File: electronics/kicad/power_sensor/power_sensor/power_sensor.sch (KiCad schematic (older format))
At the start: 6 parts, among them P4 a

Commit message: Spectrum analyzer progress
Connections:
- net at C?.1, R?.2: no longer D?.3
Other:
- moved on the sheet: C?, D?, P4, R?
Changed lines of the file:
@@
 L power:GND #PWR?
 U 1 1 5F014890
-P 5450 2300
-F 0 "#PWR?" H 5450 2300 30  0001 C CNN
-F 1 "GND" H 5450 2230 30  0001 C CNN
-F 2 "" H 5450 2300 50  0001 C CNN
-F 3 "" H 5450 2300 50  0001 C CNN
-	1    5450 2300
+P 5300 1750
+F 0 "#PWR?" H 5300 1750 30  0001 C CNN
+F 1 "GND" H 5300 1680 30  0001 C CNN
+F 2 "" H 5300 1750 50  0001 C CNN
+F 3 "" H 5300 1750 50  0001 C CNN
+	1    5300 1750
 	0    1    1    0
 $EndComp
@@
 L SparkFun-Capacitors:6PF-0402-50V-0.5% C?
 U 1 1 5F01536C
-P 6250 2500
-F 0 "C?" H 6358 2592 45  0000 L CNN
-F 1 "1 nF" H 6358 2508 45  0000 L CNN
-F 2 "0402" H 6250 2750 20  0001 C CNN
-F 3 "" H 6250 2500 50  0001 C CNN
-F 4 "" H 6358 2466 60  0000 L CNN "Field4"
-	1    6250 2500
+P 6100 1950
+F 0 "C?" H 6208 2042 45  0000 L CNN
+F 1 "1 nF" H 6208 1958 45  0000 L CNN
+F 2 "0402" H 6100 2200 20  0001 C CNN
+F 3 "" H 6100 1950 50  0001 C CNN
+F 4 "" H 6208 1916 60  0000 L CNN "Field4"
+	1    6100 1950
 	1    0    0    -1
 $EndComp
@@
 L power:GND #PWR?
 U 1 1 5F016B90
-P 6250 2600
-F 0 "#PWR?" H 6250 2600 30  0001 C CNN
-F 1 "GND" H 6250 2530 30  0001 C CNN
-F 2 "" H 6250 2600 50  0001 C CNN
-F 3 "" H 6250 2600 50  0001 C CNN
-	1    6250 2600
+P 6100 2050
+F 0 "#PWR?" H 6100 2050 30  0001 C CNN
+F 1 "GND" H 6100 1980 30  0001 C CNN
+F 2 "" H 6100 2050 50  0001 C CNN
+F 3 "" H 6100 2050 50  0001 C CNN
+	1    6100 2050
 	1    0    0    -1
 $EndComp
@@
 L conn:CONN_1 P4
 U 1 1 5EBA8EF1
-P 5750 2950
-F 0 "P4" H 5683 2853 40  0000 C CNN
-F 1 "a" H 5700 2990 30  0001 C CNN
-F 2 "TestPoint:TestPoint_Pad_1.5x1.5mm" H 5750 2950 50  0001 C CNN
-F 3 "" H 5750 2950 50  0001 C CNN
-	1    5750 2950
+P 5600 2950
+F 0 "P4" H 5533 2853 40  0000 C CNN
+F 1 "a" H 5550 2990 30  0001 C CNN
+F 2 "TestPoint:TestPoint_Pad_1.5x1.5mm" H 5600 2950 50  0001 C CNN
+F 3 "" H 5600 2950 50  0001 C CNN
+	1    5600 2950
 	0    1    1    0
 $EndComp
 Wire Wire Line
-	6250 2300 6050 2300
-Connection ~ 6250 2300
+	6100 1750 5900 1750
+Connection ~ 6100 1750
 $Comp
 L SparkFun-Resistors:RESISTOR0402 R?
 U 1 1 5F0217ED
-P 6700 2500
-F 0 "R?" V 6605 2568 45  0000 L CNN
-F 1 "10k" V 6689 2568 45  0000 L CNN
-F 2 "0402" H 6700 2650 20  0001 C CNN
-F 3 "" H 6700 2500 60  0001 C CNN
-F 4 " " V 6784 2568 60  0000 L CNN "Field4"
-	1    6700 2500
+P 6550 1950
+F 0 "R?" V 6455 2018 45  0000 L CNN
+F 1 "10k" V 6539 2018 45  0000 L CNN
+F 2 "0402" H 6550 2100 20  0001 C CNN
+F 3 "" H 6550 1950 60  0001 C CNN
+F 4 " " V 6634 2018 60  0000 L CNN "Field4"
+	1    6550 1950
 	0    1    1    0
 $EndComp
@@
 L power:GND #PWR?
 U 1 1 5F021FD0
-P 6700 2700
-F 0 "#PWR?" H 6700 2700 30  0001 C CNN
-F 1 "GND" H 6700 2630 30  0001 C CNN
-F 2 "" H 6700 2700 50  0001 C CNN
-F 3 "" H 6700 2700 50  0001 C CNN
-	1    6700 2700
+P 6550 2150
+F 0 "#PWR?" H 6550 2150 30  0001 C CNN
+F 1 "GND" H 6550 2080 30  0001 C CNN
+F 2 "" H 6550 2150 50  0001 C CNN
+F 3 "" H 6550 2150 50  0001 C CNN
+	1    6550 2150
 	1    0    0    -1
 $EndComp
 Wire Wire Line
-	6250 2300 6700 2300
+	6100 1750 6550 1750
 $Comp
 L SparkFun-Capacitors:6PF-0402-50V-0.5% C?
 U 1 1 5F022E92
-P 5750 2700
-F 0 "C?" V 5516 2750 45  0000 C CNN
-F 1 "100 pF" V 5600 2750 45  0000 C CNN
-F 2 "0402" H 5750 2950 20  0001 C CNN
-F 3 "" H 5750 2700 50  0001 C CNN
-F 4 "" H 5858 2666 60  0000 L CNN "Field4"
-	1    5750 2700
+P 5600 2700
+F 0 "C?" V 5366 2750 45  0000 C CNN
+F 1 "100 pF" V 5450 2750 45  0000 C CNN
+F 2 "0402" H 5600 2950 20  0001 C CNN
+F 3 "" H 5600 2700 50  0001 C CNN
+F 4 "" H 5708 2666 60  0000 L CNN "Field4"
+	1    5600 2700
 	1    0    0    -1
 $EndComp
@@
 L SparkFun-Resistors:0.3OHM-0805-1_8W-1% R?
 U 1 1 5F028E3F
-P 5550 2500
-F 0 "R?" H 5550 2694 45  0000 C CNN
-F 1 "50" H 5550 2610 45  0000 C CNN
-F 2 "0805" H 5550 2650 20  0001 C CNN
-F 3 "" H 5550 2500 60  0001 C CNN
-F 4 "" H 5550 2621 60  0000 C CNN "Field4"
-	1    5550 2500
+P 5400 2500
+F 0 "R?" H 5400 2694 45  0000 C CNN
+F 1 "50" H 5400 2610 45  0000 C CNN
+F 2 "0805" H 5400 2650 20  0001 C CNN
+F 3 "" H 5400 2500 60  0001 C CNN
+F 4 "" H 5400 2621 60  0000 C CNN "Field4"
+	1    5400 2500
 	1    0    0    -1
 $EndComp
@@
 L Diode:BAS40-04 D?
 U 1 1 5F013846
-P 5750 2400
-F 0 "D?" H 5750 2725 50  0000 C CNN
-F 1 "BAT15-04" H 5750 2634 50  0000 C CNN
-F 2 "Package_TO_SOT_SMD:SOT-23" H 5500 2700 50  0001 L CNN
-F 3 "http://www.vishay.com/docs/85701/bas40v.pdf" H 5630 2500 50  0001 C CNN
-	1    5750 2400
+P 5600 1850
+F 0 "D?" H 5600 2175 50  0000 C CNN
+F 1 "BAT15-04" H 5600 2084 50  0000 C CNN
+F 2 "Package_TO_SOT_SMD:SOT-23" H 5350 2150 50  0001 L CNN
+F 3 "http://www.vishay.com/docs/85701/bas40v.pdf" H 5480 1950 50  0001 C CNN
+	1    5600 1850
 	1    0    0    -1
 $EndComp
-Connection ~ 5750 2500
 $Comp
 L power:GND #PWR?
 U 1 1 5F0342F0
-P 5350 2500
-F 0 "#PWR?" H 5350 2500 30  0001 C CNN
-F 1 "GND" H 5350 2430 30  0001 C CNN
-F 2 "" H 5350 2500 50  0001 C CNN
-F 3 "" H 5350 2500 50  0001 C CNN
-	1    5350 2500
+P 5200 2500
+F 0 "#PWR?" H 5200 2500 30  0001 C CNN
+F 1 "GND" H 5200 2430 30  0001 C CNN
+F 2 "" H 5200 2500 50  0001 C CNN
+F 3 "" H 5200 2500 50  0001 C CNN
+	1    5200 2500
 	0    1    1    0
 $EndComp

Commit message: Progress
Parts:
- added C2, C4, C?: 1 nF, 0402, symbol SparkFun-Capacitors:6PF-0402-50V-0.5%
- added D1, D2, D4: BAT15-04, Package_TO_SOT_SMD:SOT-23, symbol Diode:BAS40-04
- added P1, P2, P3: a, TestPoint:TestPoint_Pad_1.5x1.5mm, symbol conn:CONN_1
- added R2, R3, R5: 10k, 0402, symbol SparkFun-Resistors:RESISTOR0402
- C1: renamed from C?; value 100 pF -> 1 nF
- gave numbers to parts that had none: 4
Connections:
- net GND: now also C1.2, C2.2, C4.2, R2.2, R3.2, R5.2
- net INP: now reaches P4.1
- net INP: now also D3.3, R1.2, D1.1, D2.3; no longer C1.2
- net at C1.1: now also D1.2, P1.1, R2.1; no longer R1.2
- new net: C2.1, D2.2, P2.1, R3.1
- new net: C4.1, D4.2, P3.1, R5.1
- new net: C?.1, D4.3
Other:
- moved on the sheet: C1, P4

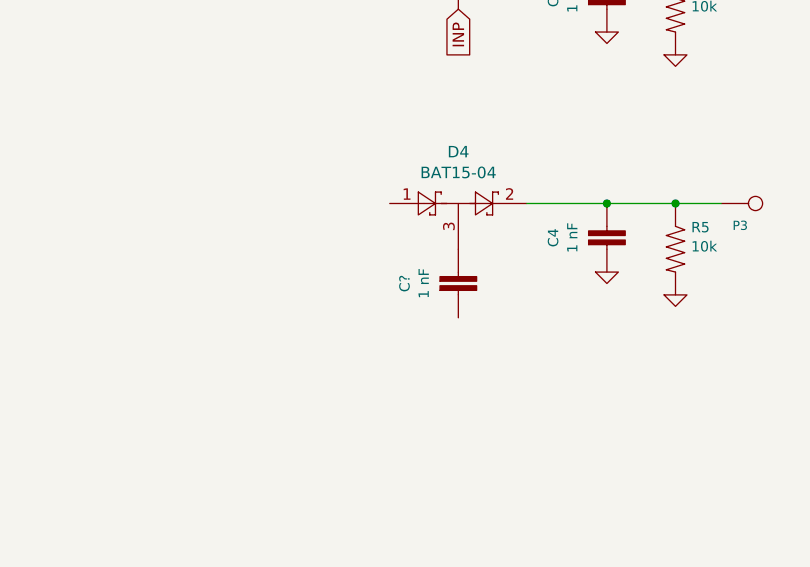
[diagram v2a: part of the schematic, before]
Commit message: Coplanar amp
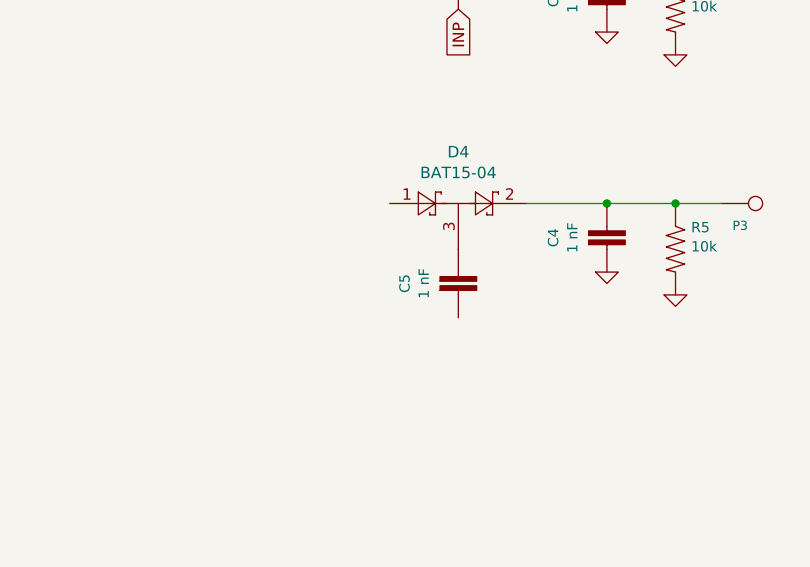
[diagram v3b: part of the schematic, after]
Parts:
- gave numbers to parts that had none: 1
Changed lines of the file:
@@
 Connection ~ 6550 4750
 $Comp
-L SparkFun-Capacitors:6PF-0402-50V-0.5% C?
+L SparkFun-Capacitors:6PF-0402-50V-0.5% C5
 U 1 1 5F339B4B
 P 5600 5150
-F 0 "C?" V 5366 5200 45  0000 C CNN
+F 0 "C5" V 5366 5200 45  0000 C CNN
 F 1 "1 nF" V 5450 5200 45  0000 C CNN
 F 2 "0402" H 5600 5400 20  0001 C CNN
